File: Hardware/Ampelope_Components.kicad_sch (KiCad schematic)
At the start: 109 parts, among them J1 Conn_01x12_Male, J18 SWD_Header, J19 USB_B_Micro, J2 Conn_01x12_Male, J3 Conn_01x12_Male, J4 Conn_01x12_Male, J5 Eurorack_16_pin_power, Q1 MMBT3906, Q2 MMBT3906, Q3 MMBT3906, Q4 MMBT3906, Q5 MMBT3906, U1 STM32G431RB, U2 AS3364, U3 LM1117-3.3, U4 TL074, U5 TL074, U6 TL074, Y1 8MHz 20pF

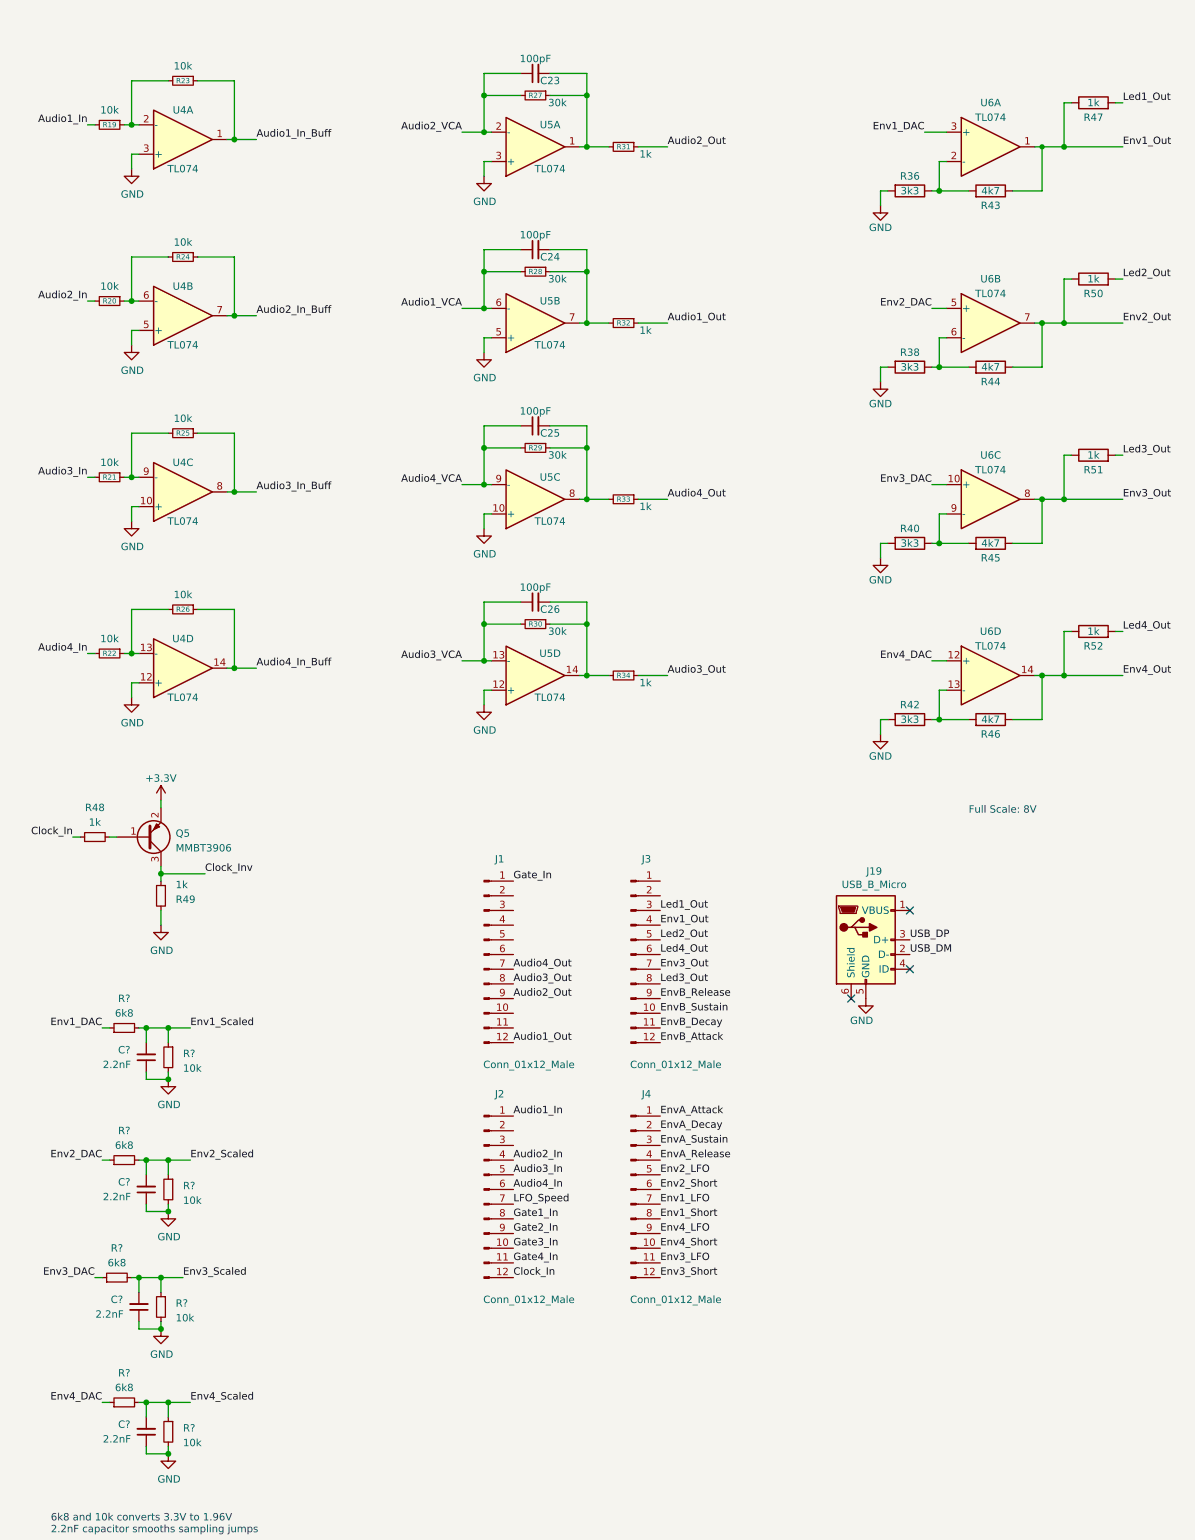
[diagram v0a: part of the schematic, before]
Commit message: Updates to component PCB to reflect VCA schematic changes
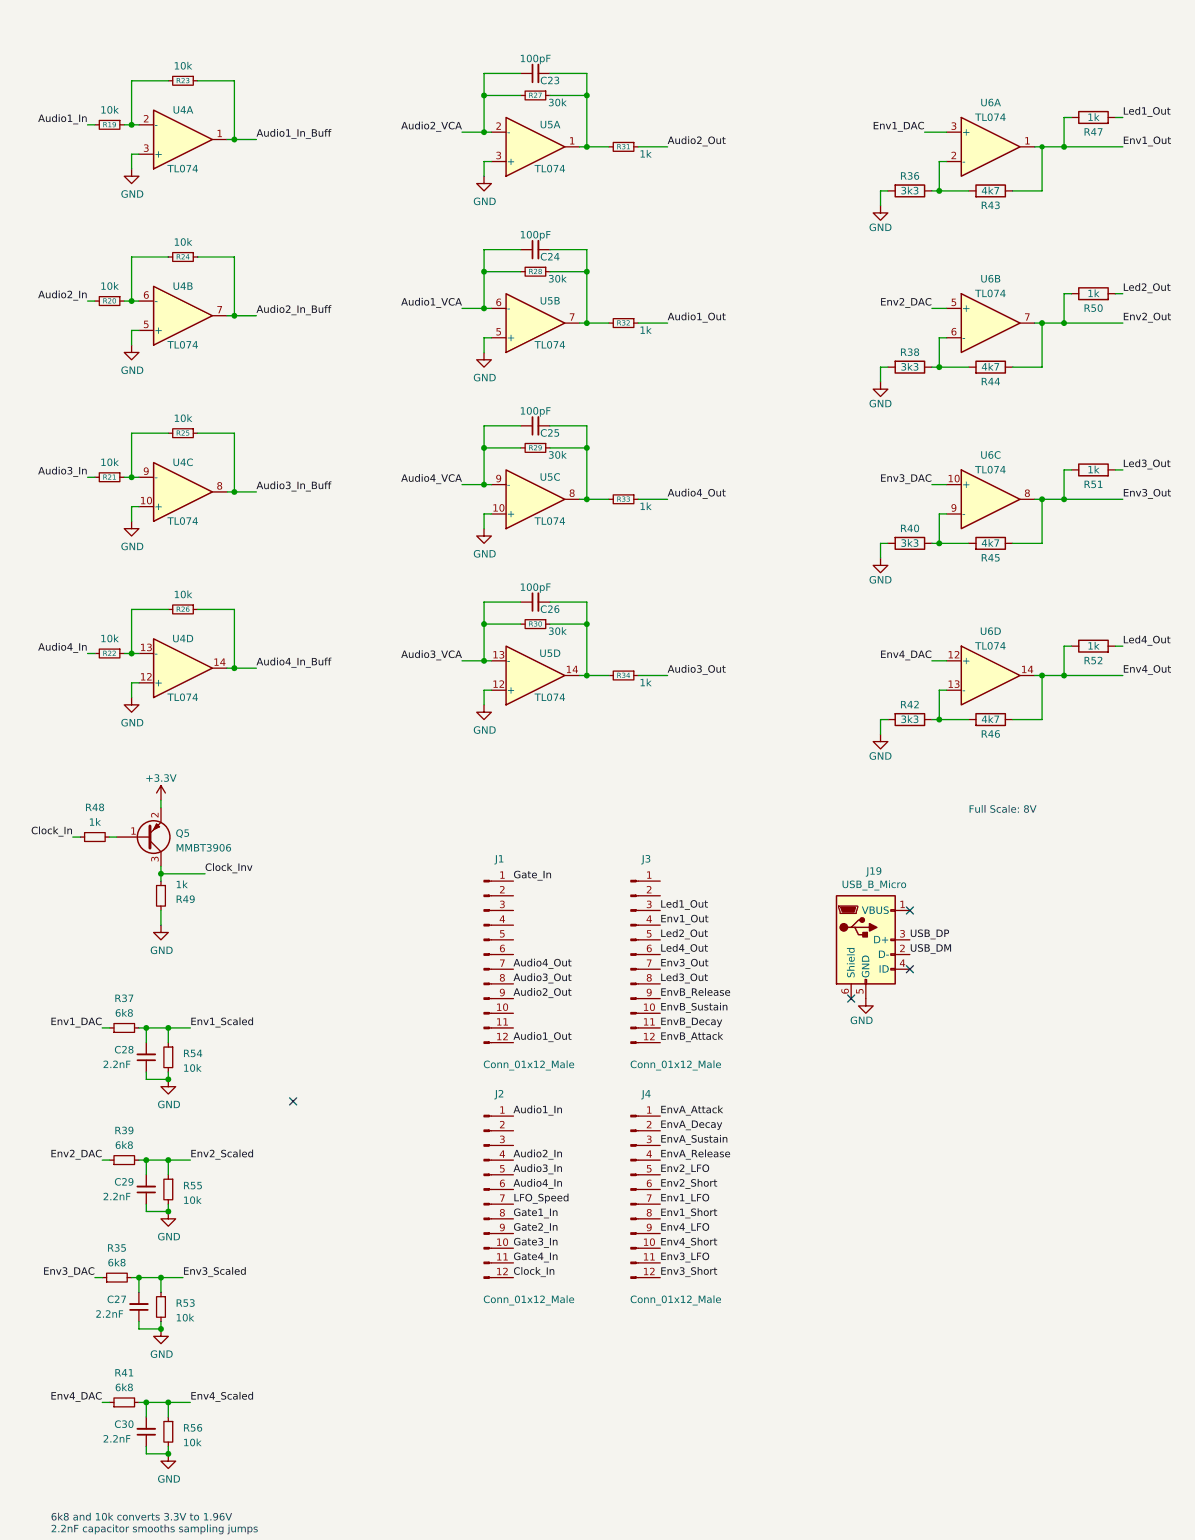
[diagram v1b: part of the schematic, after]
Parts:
- gave numbers to parts that had none: 12
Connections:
- no-connect marks 25 -> 26
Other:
- moved on the sheet: R47, R50, R51, R52

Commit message: Added test points to component PCB; Added 3D mockups
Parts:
- added FID1: 4_Layer_Marker, Custom_Footprints:4_Layer_Markers, symbol Mechanical:Fiducial
- added J6: Conn_01x02_Male, Connector_PinHeader_2.54mm:PinHeader_1x02_P2.54mm_Vertical, symbol Connector:Conn_01x02_Male
- added TP1, TP2, TP3, TP4, TP5: TestPoint, Custom_Footprints:1.3mm_Test_Point, symbol Connector:TestPoint
- renumbered J18 to J7, J19 to J8
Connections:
- net +3V3: now also J1.2 (Pin_2), J1.3 (Pin_3), J1.4 (Pin_4), J1.5 (Pin_5), TP2.1
- net Audio1_In: now also J2.2 (Pin_2); no longer J2.1 (Pin_1)
- net Audio2_In: now also J2.3 (Pin_3); no longer J2.4 (Pin_4)
- net Audio3_In: now also J2.4 (Pin_4); no longer J2.5 (Pin_5)
- net Audio4_In: now also J2.5 (Pin_5); no longer J2.6 (Pin_6)
- net Env1_LFO: now also J4.6 (Pin_6), U1.59 (PB6); no longer J4.7 (Pin_7), U1.57 (PB4)
- net Env1_Short: now also J4.7 (Pin_7), U1.58 (PB5); no longer J4.8 (Pin_8), U1.56 (PB3)
- net Env2_LFO: now also J4.8 (Pin_8), U1.57 (PB4); no longer J4.5 (Pin_5), U1.59 (PB6)
- net Env2_Short: now also J4.9 (Pin_9), U1.56 (PB3); no longer J4.6 (Pin_6), U1.58 (PB5)
- net Env3_LFO: now also J4.10 (Pin_10), U1.54 (PC12); no longer J4.11 (Pin_11), U1.52 (PC10)
- net Env3_Short: now also J4.11 (Pin_11), U1.52 (PC10); no longer J4.12 (Pin_12), U1.51 (PA15)
- net Env4_LFO: now also J4.12 (Pin_12), U1.51 (PA15); no longer J4.9 (Pin_9), U1.54 (PC12)
- net Env4_Short: now also J2.7 (Pin_7), U1.34 (PB12); no longer J4.10 (Pin_10), U1.53 (PC11)
- net GND: now also J1.10 (Pin_10), J1.11 (Pin_11), J1.6 (Pin_6), J2.1 (Pin_1), J3.1 (Pin_1), J3.2 (Pin_2), J4.5 (Pin_5), TP1.1, TP5.1
- net Gate1_Inv: now also U1.35 (PB13); no longer U1.34 (PB12)
- net Gate2_Inv: now also U1.36 (PB14); no longer U1.35 (PB13)
- net Gate3_Inv: now also U1.37 (PB15); no longer U1.36 (PB14)
- net Gate4_Inv: now also U1.38 (PC6); no longer U1.37 (PB15)
- net LFO_Speed: now also J2.6 (Pin_6); no longer J2.7 (Pin_7)
- net VCC: now also TP3.1
- net VEE: now also TP4.1
- net UART3_TX: now reaches U1.62 (PB9)
- net UART3_TX: now also J6.1 (Pin_1)
- new net UART3_RX: J6.2 (Pin_2), U1.53 (PC11)
- no-connect marks 26 -> 23
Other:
- note added: "6k8 and 10k converts 3.3V to 1.96V (max output of VCA) 2.2nF capacitor smooths sampling steps"
- note added: "Audio Buffers and Envelope Amplifiers"
- note added: "Connectors"
- note added: "DAC Envelope scaling for VCA"
- note added: "Input protection"
- note added: "MCU"
- note added: "Power Supply"
- note added: "Quad Linear VCA"
- note removed: "6k8 and 10k converts 3.3V to 1.96V 2.2nF capacitor smooths sampling jumps"
- note removed: "Class AB (best noise performance) Pin 1 left open Class A (lowest distortion) resistor between Pin 1 and V+. NB SSI2164 recommends 20k, 220R and 1.2nF for RC components"
- note removed: "TODO: - Serial debug points - Power test points"
- company: (none) -> Mountjoy Modular
- title: (none) -> Ampelope Component Board
- moved on the sheet: C1, C10, C11, C12, C13, C14, C15, C16, C17, C18, C19, C2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

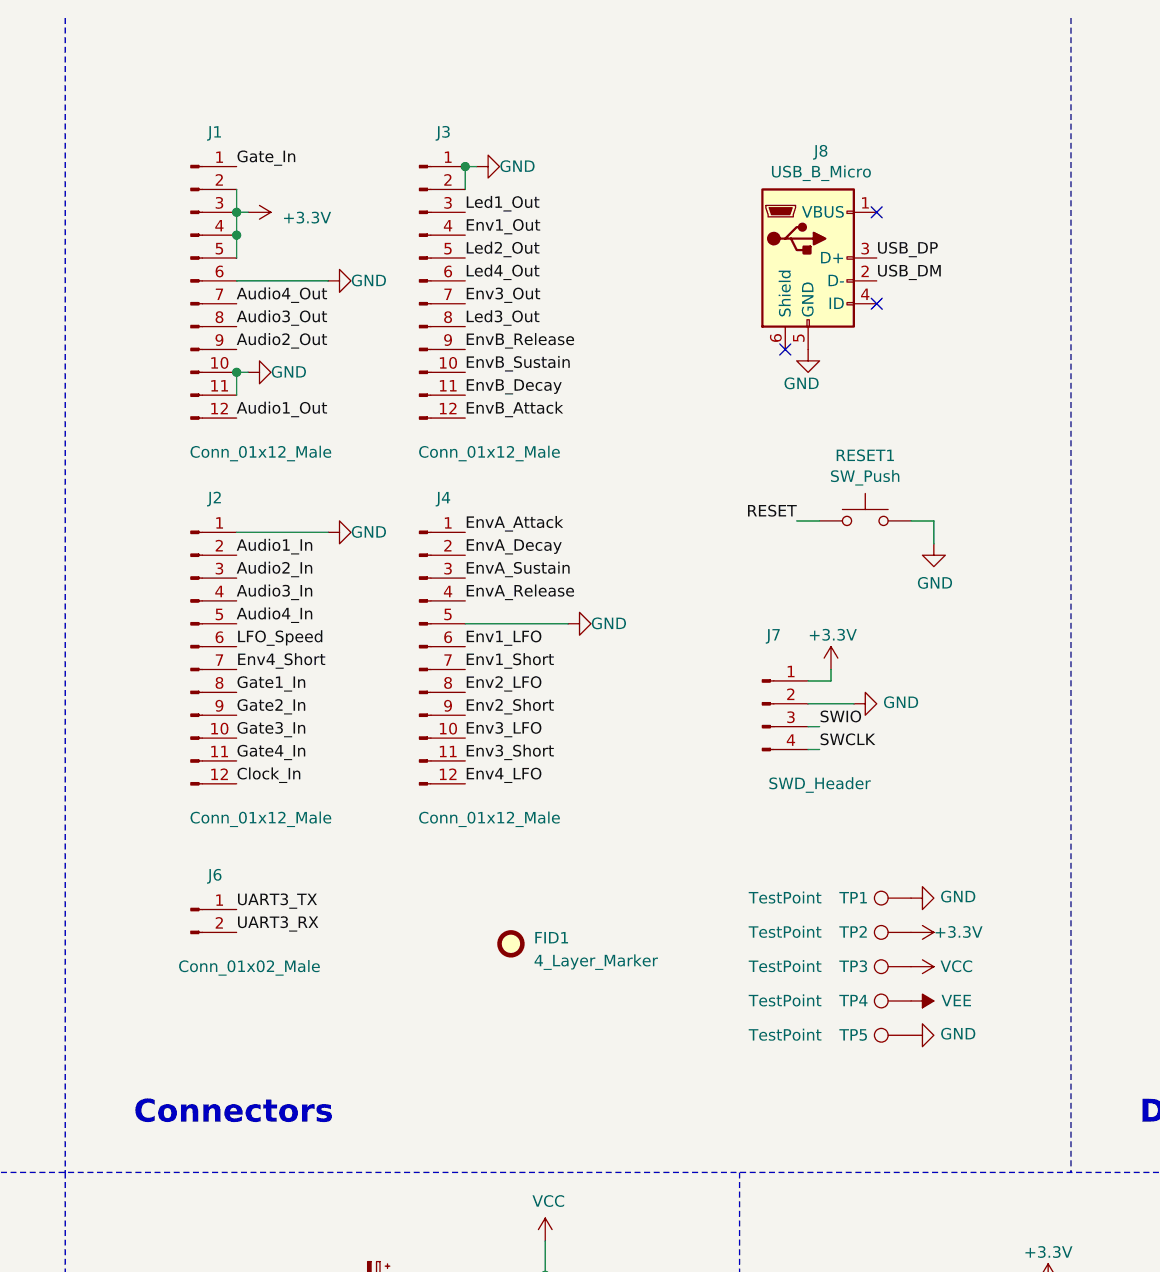
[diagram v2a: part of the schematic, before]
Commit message: Fixed DRC errors on control and component boards
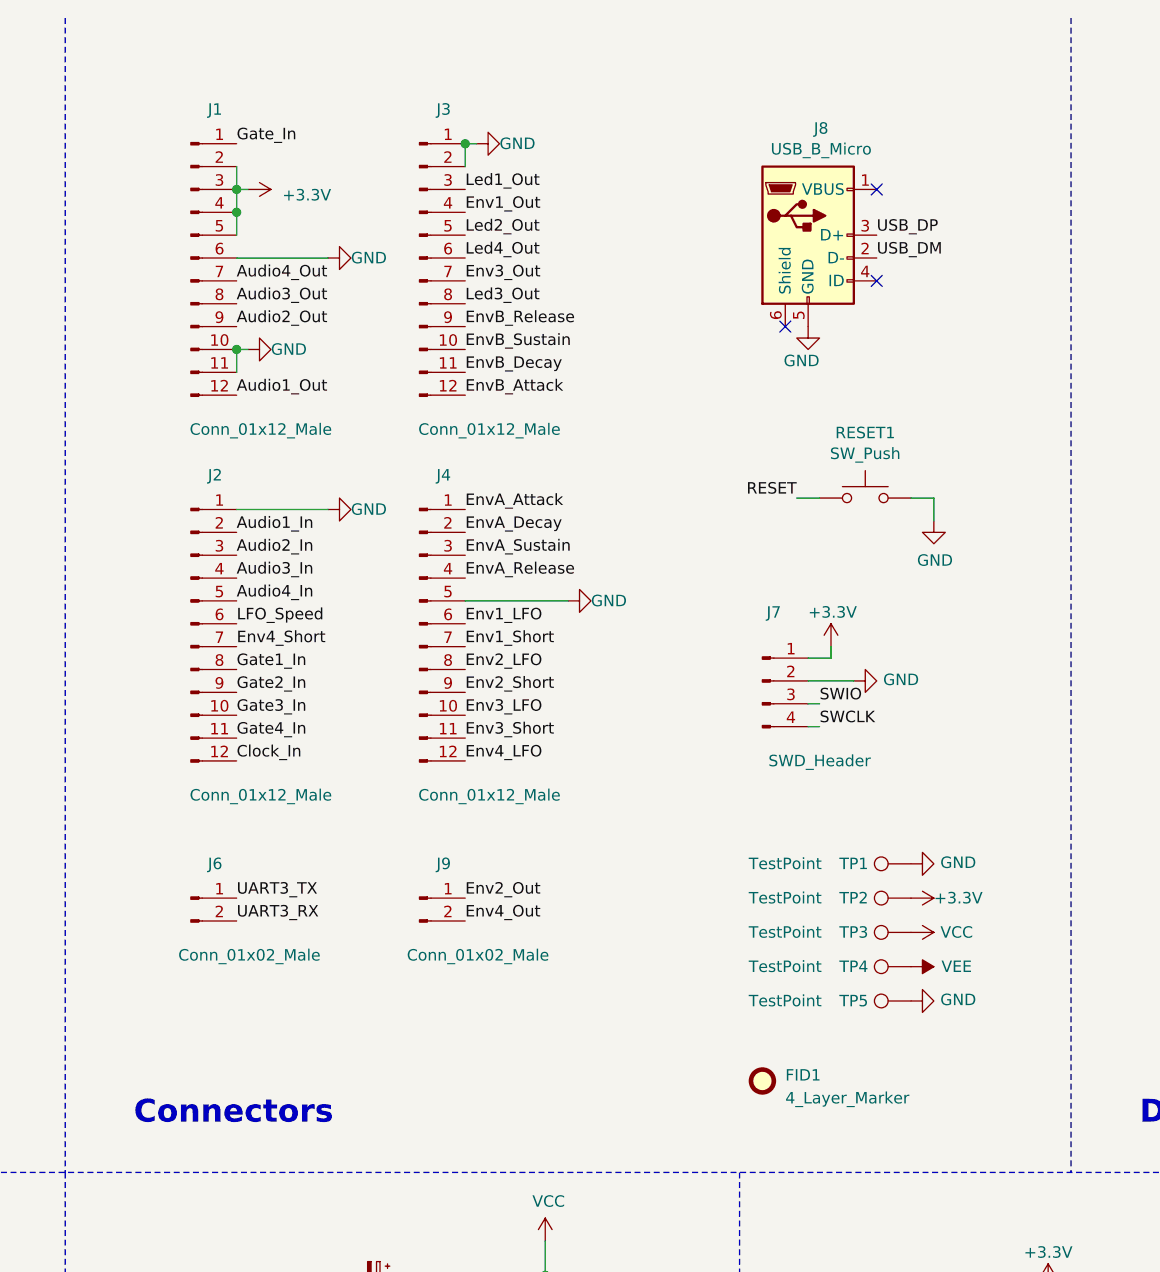
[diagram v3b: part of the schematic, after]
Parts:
- added J9: Conn_01x02_Male, Connector_PinHeader_2.54mm:PinHeader_1x02_P2.54mm_Vertical, symbol Connector:Conn_01x02_Male
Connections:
- net Env2_Out: now also J9.1 (Pin_1)
- net Env4_Out: now also J9.2 (Pin_2)
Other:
- moved on the sheet: FID1, J1, J2, J3, J4, J6, J7, J8, RESET1, TP1, TP2, TP3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
